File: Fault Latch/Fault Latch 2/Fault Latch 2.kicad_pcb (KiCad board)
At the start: 2 copper layers, 85 x 85 mm, 108 parts, among them J1 1053141312, J3 1053131202, J4 1053131202, K101 Fujitsu_FTR-LYAA005x, K102 Fujitsu_FTR-LYAA005x, K103 Fujitsu_FTR-LYAA005x, Q101 Q_NPN_BEC, Q102 Q_NPN_BEC, Q103 Q_NPN_BEC, Q104 Q_NPN_BEC, Q105 Q_NMOS_GSD, Q106 Q_NMOS_GSD, Q107 Q_PMOS_GSD, Q108 Q_PMOS_GSD, Q109 Q_PMOS_GSD, Q110 Q_NPN_BEC, Q111 Q_NPN_BEC, Q112 Q_NMOS_GSD, Q113 Q_PMOS_GSD, Q114 Q_NMOS_GSD, Q115 Q_NMOS_GSD, Q116 Q_NMOS_GSD, SW101 SW_Omron_B3FS, SW102 SW_Omron_B3FS, SW103 SW_Omron_B3FS, U101 SFH617A-1, U102 SFH617A-1, U103 SFH617A-1, U104 74AHC1G00, U105 74AHC1G00, U106 74AHC1G00, U107 74LS279, U109 SFH617A-1, U110 SFH617A-1, U117 74AHC1G00, U118 LM555xM, U119 74AHC1G00, U121 SFH617A-1, U2 LM1117DT-5.0

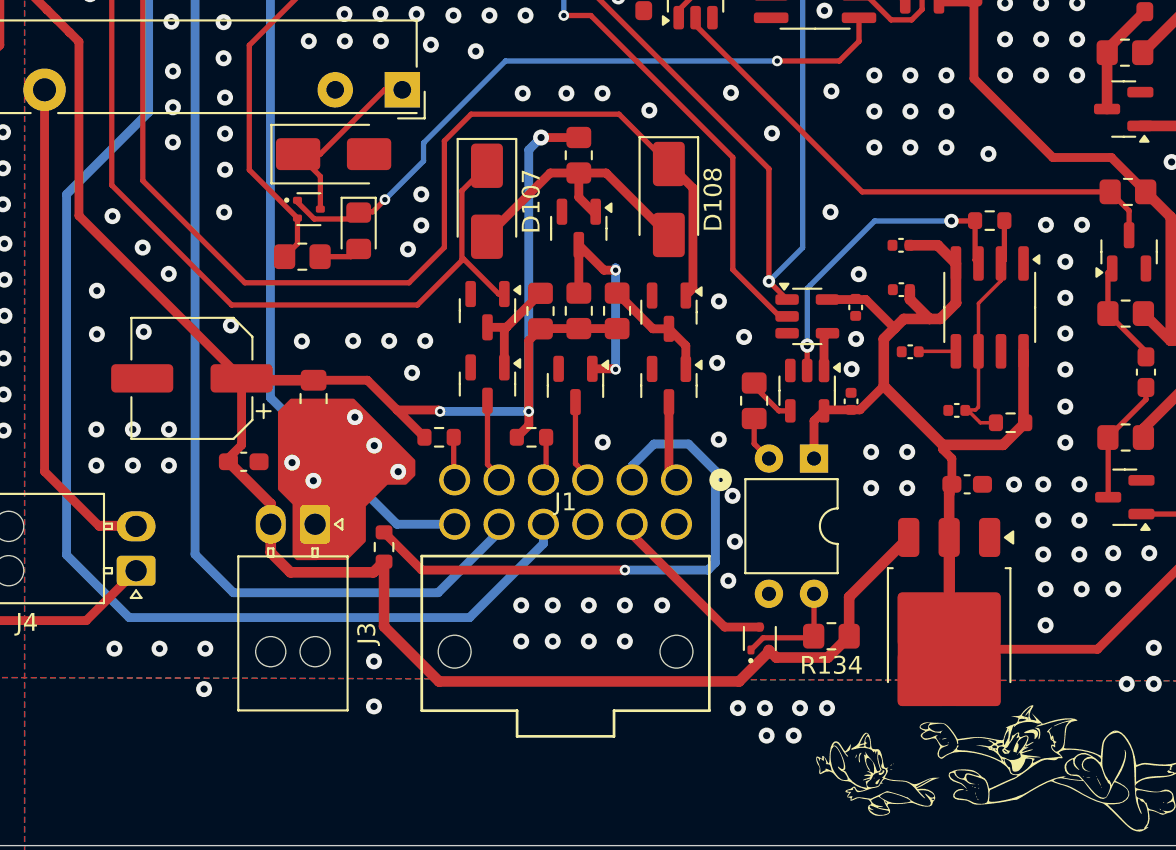
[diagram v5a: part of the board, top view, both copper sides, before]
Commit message: Fault Latch pre-BOM check
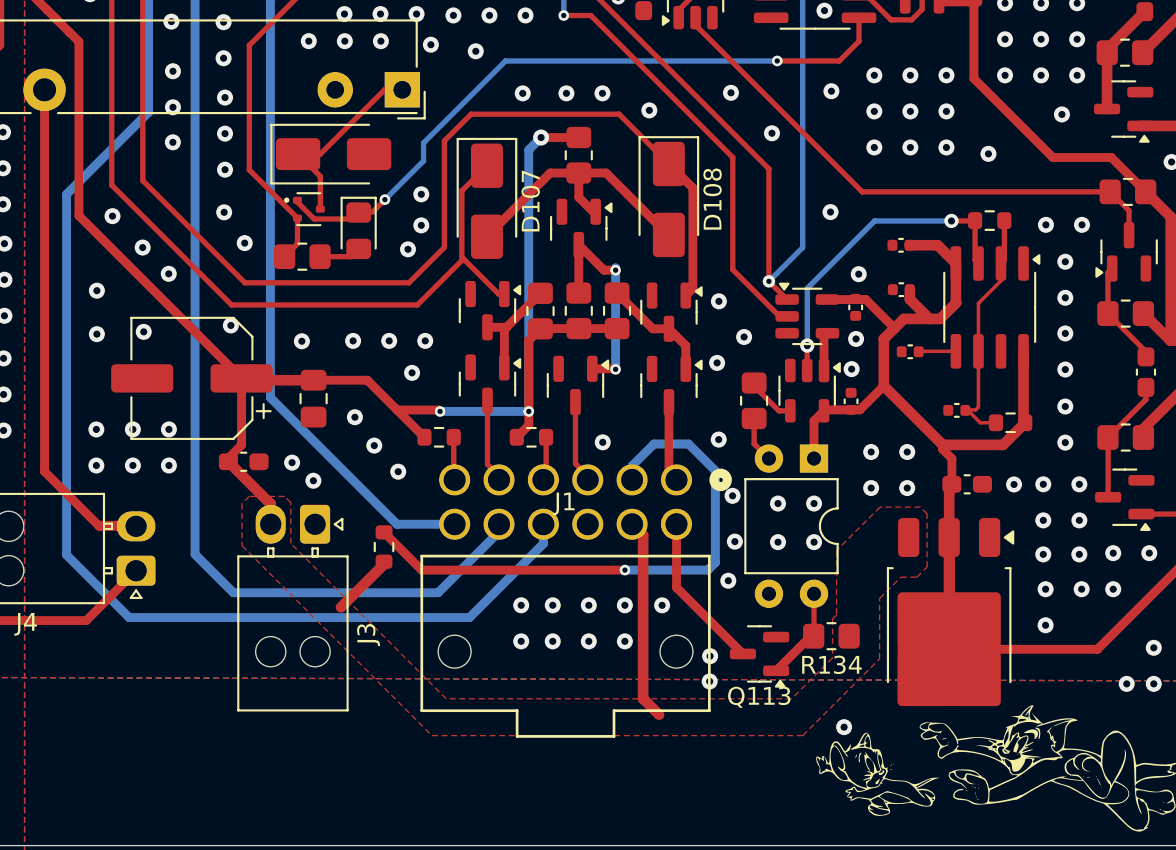
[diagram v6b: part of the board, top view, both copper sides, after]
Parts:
- Q113: value Q_PMOS_GSD -> Q_NMOS_GSD; footprint Package_TO_SOT_SMD:SOT-523 -> Package_TO_SOT_SMD:SOT-23
- moved Q113 0.87 mm to (241.0, 119.5), turned to 180 degrees
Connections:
- J1 pad 7: GND -> /TSSI Red Out
- J1 pad 8: /TSSI Red In -> +12V
- Q113 pad 2: +12V -> GND
- Q113 pad 3: /TSSI Red In -> /TSSI Red Out
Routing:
- net +12V: track 203.0 -> 169.7 mm
- net /TSSI Red In: track 10.2 -> 0.00 mm
- net /TSSI Red Out: track 0.00 -> 8.86 mm
- net Net-(Q113-G): track 6.25 -> 5.45 mm
- net GND: vias 367 -> 364
- added copper zone on F.Cu, net +12V

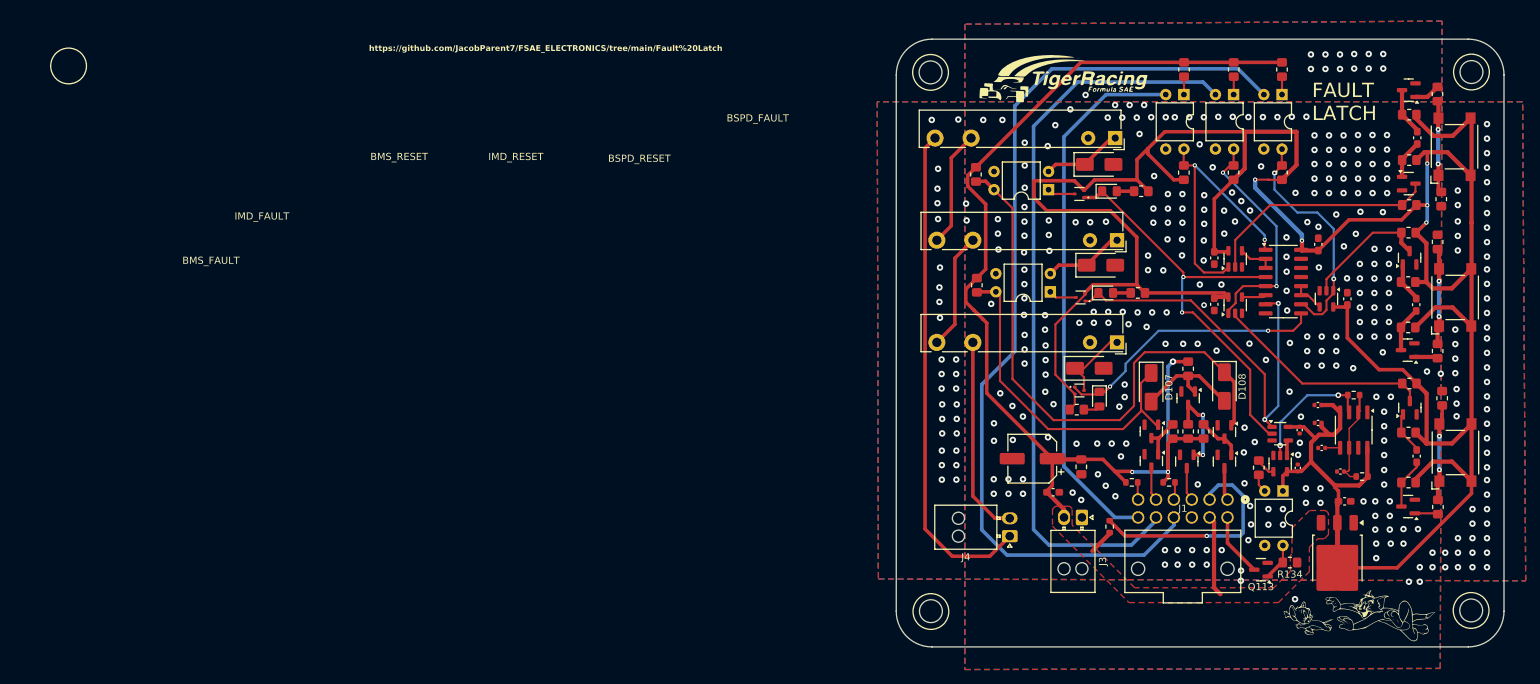
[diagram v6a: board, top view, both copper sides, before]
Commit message: Fault Latch BOM Checked and Safety Circuit
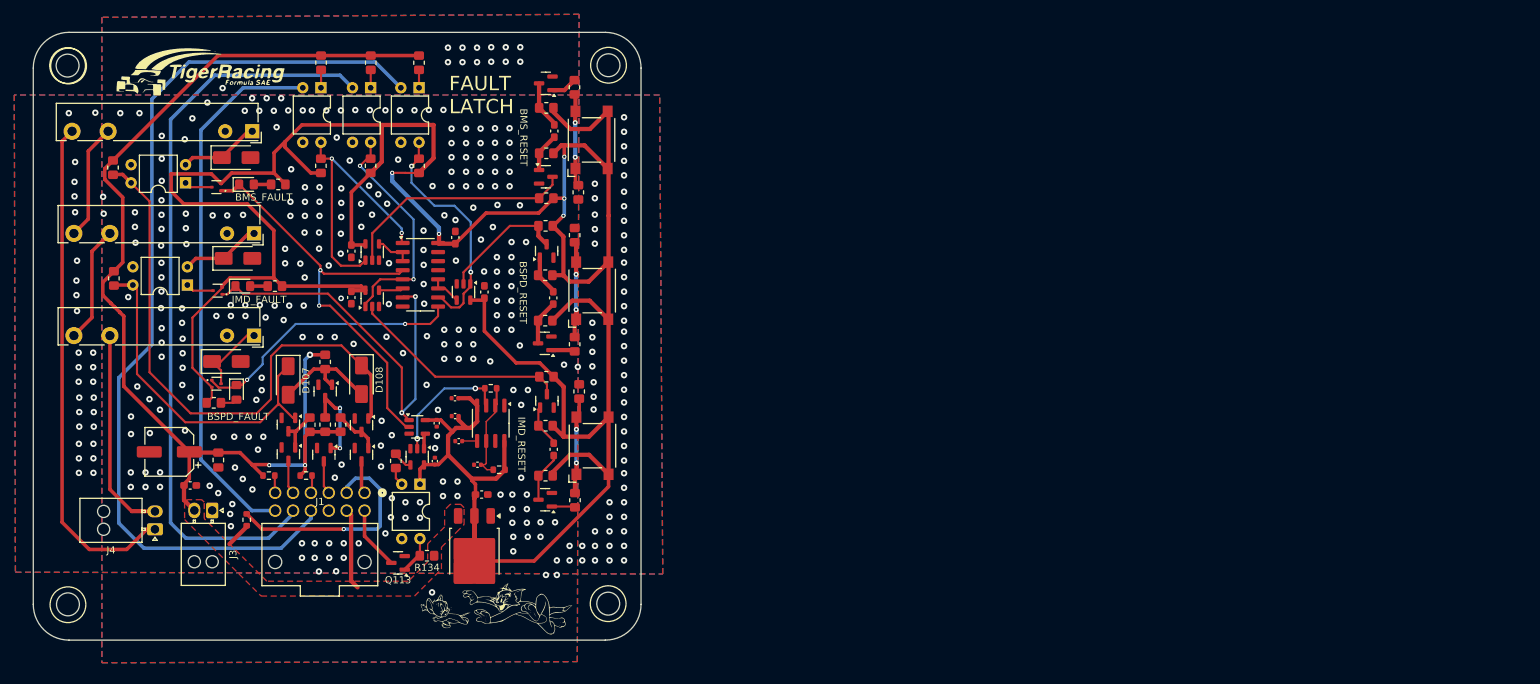
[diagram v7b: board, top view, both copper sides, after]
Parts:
- moved J3 121.6 mm to (94.3, 111.2)
- moved C105 120.7 mm to (142.1, 102.7)
- moved C107 120.7 mm to (128.3, 98.0)
- moved C109 120.7 mm to (128.8, 101.5)
- moved H104 120.7 mm to (149.7, 49.0)
- moved R105 120.7 mm to (145.0, 52.1)
- moved R129 120.7 mm to (140.9, 71.4)
- moved SW103 120.7 mm to (147.5, 80.5)
- moved C114 120.7 mm to (95.2, 104.2)
- moved D107 120.7 mm to (104.9, 93.1)
- moved D108 120.7 mm to (115.2, 93.0)
- moved G*** 120.7 mm to (84.4, 51.4)
- moved J1 120.7 mm to (115.6, 108.8)
- moved Q116 120.7 mm to (110.1, 94.6)
- moved R102 120.7 mm to (109.5, 48.6)
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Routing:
- net /Shutdown Circuit Out: track 29.5 -> 31.0 mm
- net /Shutdown Circuit In: track 69.8 -> 71.0 mm
- net GND: vias 364 -> 355
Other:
- board text removed: "https://github.com/JacobParent7/FSAE_ELECTRONICS/tree/main/Fault%20Latch"
